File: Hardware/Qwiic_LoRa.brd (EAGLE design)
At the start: 66 x 40.3 mm, 57 parts, among them J1 Qwiic Right Angle, J2 Qwiic Right Angle, J4 AVR_SPI_PROG_3X2TESTPOINTS, J5 U.FL, U1 ATMEGA328P_TQFP, U2 RFM96W, Y1 16MHz

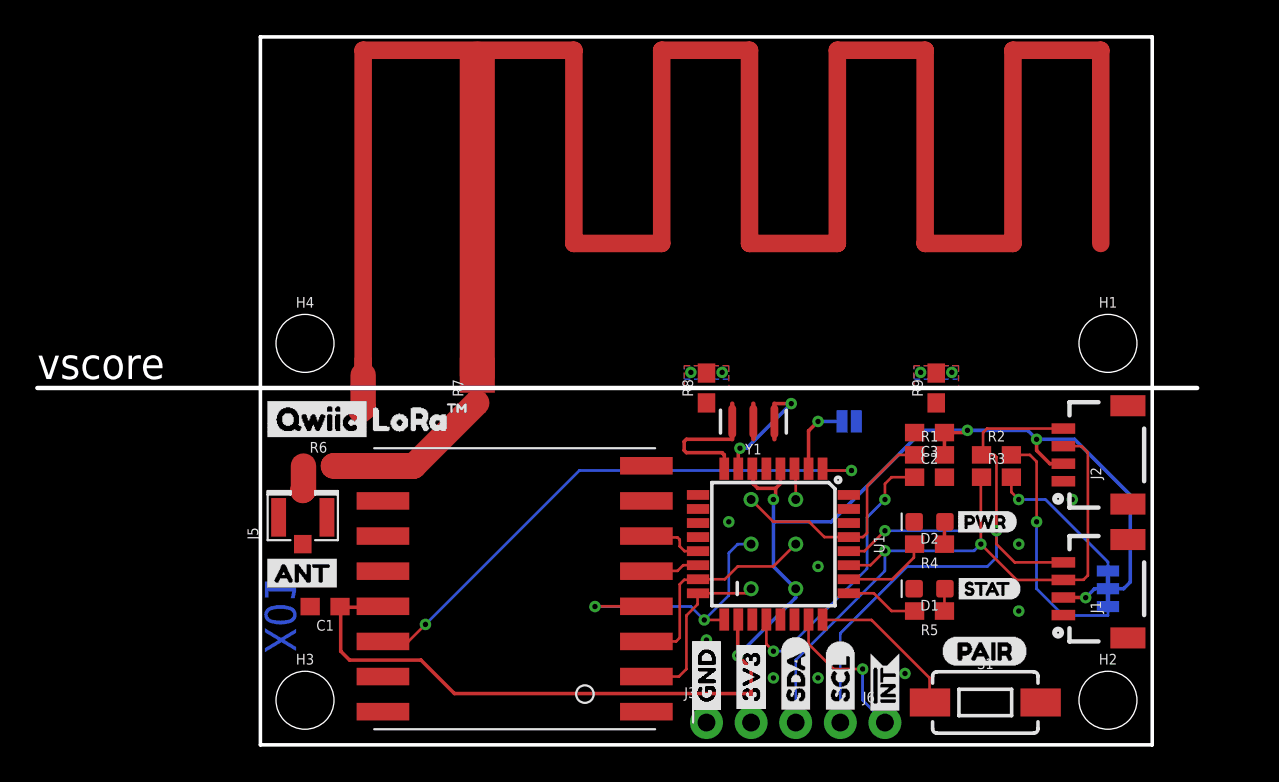
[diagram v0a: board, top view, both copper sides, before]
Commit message: x02
- Trim Antenna
- Silkscreen Changes to Comply with Semtech TM Requirements
- Adjust Mounting Holse to Mount to Qwiic Shield + Arduino R3
- Route DIO1 and DIO2 from RFM95
- Add Serial Debug Testpoints
- Add DNP for Shunt Components
- Add GND Leg Landing for Antenna Footprint
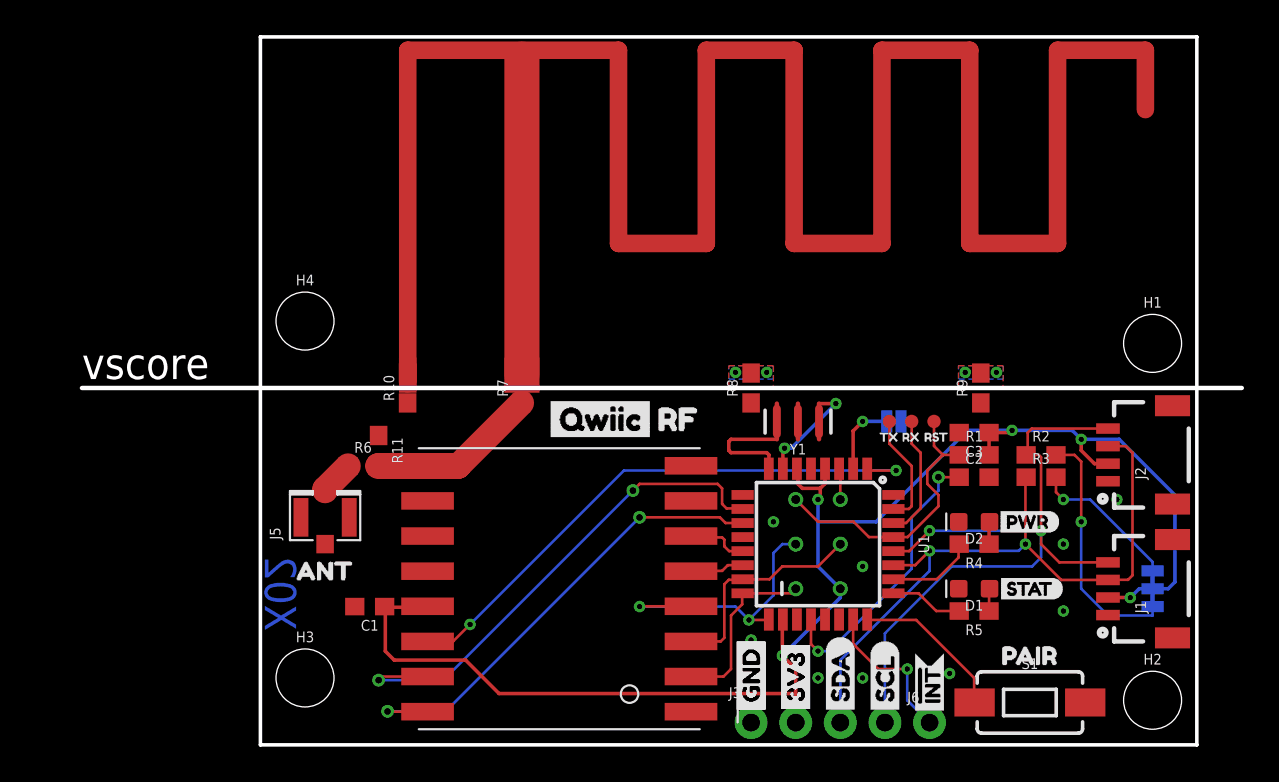
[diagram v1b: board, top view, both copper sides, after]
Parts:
- added R10: 0, SparkFun-Resistors:0603
- added R11: DNP, SparkFun-Resistors:0603
- added TP1, TP2, TP3: (no value), SparkFun-Connectors:PAD.03X.03
- added U$27: (no value), buzzard_labels (32):RX0
- added U$28: (no value), buzzard_labels (32):RST2
- J4: value AVR_SPI_PROG_3X2TESTPOINTS -> AVR_SPI_PROG
- U$10: device lora_mark#PNG (2):LORA_MARK#PNG -> Labels:QWIIC-LOGO-SMALL
- U$11: device Labels:QWIIC-LOGO-MEDIUM -> buzzard_labels (32):TX1
- U$15: device buzzard_labels (7):LORA0 -> buzzard_labels (29):RF1
- U$17: device buzzard_labels (7):TM1 -> lora_mark#PNG (3):LORA_MARK#PNG
- U$2: device buzzard_labels:ANT3 -> buzzard_labels (30):ANT0
- U$3: device buzzard_labels:PAIR0 -> buzzard_labels (30):PAIR1
- moved U$11 29.7 mm to (34.8, 17.5), flipped to the top
- moved U$15 16.3 mm to (21.5, 18.5)
- moved U$16 16.1 mm to (15.9, 18.5)
- moved FRAME1 14.2 mm to (20.3, -10.2)
- moved U$10 13.8 mm to (9.02, 2.92)
- moved U$17 7.53 mm to (2.67, 18.4), flipped to the bottom
- moved U$13 2.85 mm to (17.0, 2.67)
- moved U$3 2.55 mm to (41.3, 5.08)
- moved R2 2.54 mm to (44.5, 16.5)
- moved R3 2.54 mm to (44.5, 15.2)
- moved U$25 2.54 mm to (48.5, 6.99)
- moved J3 2.54 mm to (27.9, 1.27)
- moved R8 2.54 mm to (27.9, 20.3)
- moved U$18 2.54 mm to (27.9, 1.52)
- moved U$19 2.54 mm to (27.9, 1.52)
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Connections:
- removed net N$10: R6.2, R7.1
- new net N$11: R10.2, U$1.GND
- new net RFM_DIO1: U1.10, U2.DIO1
- new net RFM_DIO2: U1.11, U2.DIO2
- new net RX: TP1.P$1, U1.30
- new net TX: TP2.P$1, U1.31
- net ANT: now also R11.2, R6.2, R7.1
- net GND: now also R10.1, R11.1; no longer U$1.GND
- net RST: now also TP3.P$1
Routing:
- net RFM_DIO1: track 0.00 -> 29.3 mm, vias 0 -> 2
- net RFM_DIO2: track 0.00 -> 27.2 mm, vias 0 -> 2
- net ANT: track 4.57 -> 14.3 mm
- net N$10: track 9.66 -> 0.00 mm
- net RX: track 0.00 -> 7.06 mm
- net TX: track 0.00 -> 6.46 mm
- net RST: track 13.7 -> 16.3 mm
- net GND: track 3.84 -> 1.78 mm
- net N$9: track 1.41 -> 1.94 mm
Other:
- outline, holes or cut-outs redrawn
- board text added: "NPoole 2018"
- board text added: "X02"
- board text removed: "X01"

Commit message: Version X03
Add Chip Select pullup on the radio module, only affects programming.
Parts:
- added R12: 10k, SparkFun-Resistors:0603
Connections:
- net 3.3V: now also R12.2
- net RFM_CS: now also R12.1
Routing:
- net RFM_CS: track 3.08 -> 23.8 mm
- net 3.3V: track 88.8 -> 90.3 mm
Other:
- board text added: "X03"
- board text removed: "X02"
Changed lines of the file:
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@@
 <layer number="23" name="tOrigins" color="15" fill="1" visible="yes" active="yes"/>
 <layer number="24" name="bOrigins" color="15" fill="1" visible="yes" active="yes"/>
-<layer number="25" name="tNames" color="7" fill="1" visible="no" active="yes"/>
-<layer number="26" name="bNames" color="7" fill="1" visible="no" active="yes"/>
-<layer number="27" name="tValues" color="7" fill="1" visible="no" active="yes"/>
-<layer number="28" name="bValues" color="7" fill="1" visible="no" active="yes"/>
-<layer number="29" name="tStop" color="7" fill="3" visible="no" active="yes"/>
-<layer number="30" name="bStop" color="7" fill="6" visible="no" active="yes"/>
-<layer number="31" name="tCream" color="7" fill="4" visible="no" active="yes"/>
-<layer number="32" name="bCream" color="7" fill="5" visible="no" active="yes"/>
-<layer number="33" name="tFinish" color="6" fill="3" visible="no" active="yes"/>
-<layer number="34" name="bFinish" color="6" fill="6" visible="no" active="yes"/>
-<layer number="35" name="tGlue" color="7" fill="4" visible="no" active="yes"/>
-<layer number="36" name="bGlue" color="7" fill="5" visible="no" active="yes"/>
-<layer number="37" name="tTest" color="7" fill="1" visible="no" active="yes"/>
-<layer number="38" name="bTest" color="7" fill="1" visible="no" active="yes"/>
-<layer number="39" name="tKeepout" color="4" fill="11" visible="no" active="yes"/>
-<layer number="40" name="bKeepout" color="1" fill="11" visible="no" active="yes"/>
-<layer number="41" name="tRestrict" color="4" fill="10" visible="no" active="yes"/>
-<layer number="42" name="bRestrict" color="1" fill="10" visible="no" active="yes"/>
-<layer number="43" name="vRestrict" color="2" fill="10" visible="no" active="yes"/>
-<layer number="44" name="Drills" color="7" fill="1" visible="no" active="yes"/>
+<layer number="25" name="tNames" color="7" fill="1" visible="yes" active="yes"/>
+<layer number="26" name="bNames" color="7" fill="1" visible="yes" active="yes"/>
+<layer number="27" name="tValues" color="7" fill="1" visible="yes" active="yes"/>
+<layer number="28" name="bValues" color="7" fill="1" visible="yes" active="yes"/>
+<layer number="29" name="tStop" color="7" fill="3" visible="yes" active="yes"/>
+<layer number="30" name="bStop" color="7" fill="6" visible="yes" active="yes"/>
+<layer number="31" name="tCream" color="7" fill="4" visible="yes" active="yes"/>
+<layer number="32" name="bCream" color="7" fill="5" visible="yes" active="yes"/>
+<layer number="33" name="tFinish" color="6" fill="3" visible="yes" active="yes"/>
+<layer number="34" name="bFinish" color="6" fill="6" visible="yes" active="yes"/>
+<layer number="35" name="tGlue" color="7" fill="4" visible="yes" active="yes"/>
+<layer number="36" name="bGlue" color="7" fill="5" visible="yes" active="yes"/>
+<layer number="37" name="tTest" color="7" fill="1" visible="yes" active="yes"/>
+<layer number="38" name="bTest" color="7" fill="1" visible="yes" active="yes"/>
+<layer number="39" name="tKeepout" color="4" fill="11" visible="yes" active="yes"/>
+<layer number="40" name="bKeepout" color="1" fill="11" visible="yes" active="yes"/>
+<layer number="41" name="tRestrict" color="4" fill="10" visible="yes" active="yes"/>
+<layer number="42" name="bRestrict" color="1" fill="10" visible="yes" active="yes"/>
+<layer number="43" name="vRestrict" color="2" fill="10" visible="yes" active="yes"/>
+<layer number="44" name="Drills" color="7" fill="1" visible="yes" active="yes"/>
 <layer number="45" name="Holes" color="7" fill="1" visible="yes" active="yes"/>
 <layer number="46" name="Milling" color="3" fill="1" visible="yes" active="yes"/>
-<layer number="47" name="Measures" color="7" fill="1" visible="no" active="yes"/>
-<layer number="48" name="Document" color="7" fill="1" visible="no" active="yes"/>
-<layer number="49" name="Reference" color="7" fill="1" visible="no" active="yes"/>
-<layer number="50" name="dxf" color="7" fill="1" visible="no" active="yes"/>
+<layer number="47" name="Measures" color="7" fill="1" visible="yes" active="yes"/>
+<layer number="48" name="Document" color="7" fill="1" visible="yes" active="yes"/>
+<layer number="49" name="Reference" color="7" fill="1" visible="yes" active="yes"/>
+<layer number="50" name="dxf" color="7" fill="1" visible="yes" active="yes"/>
 <layer number="51" name="tDocu" color="6" fill="1" visible="yes" active="yes"/>
-<layer number="52" name="bDocu" color="7" fill="1" visible="no" active="yes"/>
+<layer number="52" name="bDocu" color="7" fill="1" visible="yes" active="yes"/>
 <layer number="91" name="Nets" color="2" fill="1" visible="no" active="no"/>
 <layer number="92" name="Busses" color="1" fill="1" visible="no" active="no"/>
@@
 <layer number="59" name="tCarbon" color="7" fill="1" visible="no" active="no"/>
 <layer number="60" name="bCarbon" color="7" fill="1" visible="no" active="no"/>
-<layer number="88" name="SimResults" color="9" fill="1" visible="no" active="yes"/>
-<layer number="89" name="SimProbes" color="9" fill="1" visible="no" active="yes"/>
+<layer number="88" name="SimResults" color="9" fill="1" visible="yes" active="yes"/>
+<layer number="89" name="SimProbes" color="9" fill="1" visible="yes" active="yes"/>
 <layer number="90" name="Modules" color="5" fill="1" visible="no" active="no"/>
 <layer number="97" name="Info" color="7" fill="1" visible="no" active="no"/>
@@
 <wire x1="55.88" y1="20.32" x2="-10.16" y2="20.32" width="0.254" layer="46"/>
 <text x="-10.16" y="20.828" size="1.778" layer="46" font="vector" ratio="15">vscore</text>
-<text x="0.254" y="6.477" size="1.778" layer="16" font="vector" ratio="15" rot="MR90">X02</text>
+<text x="0.254" y="6.477" size="1.778" layer="16" font="vector" ratio="15" rot="MR90">X03</text>
 <text x="11.43" y="6.35" size="1.778" layer="51" font="vector" ratio="15">RFM95W
 915MHz</text>
@@
 <element name="U$27" library="buzzard_labels (32)" package="RX0" value="" x="36.068" y="17.526"/>
 <element name="U$28" library="buzzard_labels (32)" package="RST2" value="" x="37.338" y="17.526"/>
+<element name="R12" library="SparkFun-Resistors" package="0603" value="10k" x="6.223" y="9.398">
+<attribute name="PROD_ID" value="RES-00824" x="6.223" y="9.398" size="1.778" layer="27" font="vector" ratio="15" display="off"/>
+</element>
 </elements>
 <signals>
@@
 <wire x1="42.799" y1="17.907" x2="46.228" y2="17.907" width="0.2032" layer="16"/>
 <wire x1="46.228" y1="17.907" x2="46.736" y2="17.399" width="0.2032" layer="16"/>
+<contactref element="R12" pad="2"/>
+<wire x1="7.073" y1="9.398" x2="7.073" y2="7.874" width="0.1524" layer="1"/>
 </signal>
 <signal name="GND">
@@
 <wire x1="26.289" y1="9.906" x2="24.534" y2="9.906" width="0.1524" layer="1"/>
 <wire x1="24.534" y1="9.906" x2="24.518" y2="9.89" width="0.1524" layer="1"/>
+<contactref element="R12" pad="1"/>
+<wire x1="5.373" y1="9.398" x2="5.373" y2="10.199" width="0.1524" layer="1"/>
+<wire x1="5.373" y1="10.199" x2="6.096" y2="10.922" width="0.1524" layer="1"/>
+<wire x1="6.096" y1="10.922" x2="21.209" y2="10.922" width="0.1524" layer="1"/>
+<wire x1="21.209" y1="10.922" x2="22.225" y2="9.906" width="0.1524" layer="1"/>
+<wire x1="22.225" y1="9.906" x2="24.502" y2="9.906" width="0.1524" layer="1"/>
+<wire x1="24.502" y1="9.906" x2="24.518" y2="9.89" width="0.1524" layer="1"/>
 </signal>
 <signal name="RFM_RST">
